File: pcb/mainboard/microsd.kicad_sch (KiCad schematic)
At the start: 11 parts, among them U700 W25Q128JVP

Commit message: Working on mainboard schematics
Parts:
- removed U?: NX3P1108UK, footprint:CSP-4_2x2_1.0x1.0mm, symbol symbols:NX3P1108UK
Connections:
- net +3V3 is gone; now on net +SD: C?.1
- net GND is gone; now on net +SD: C701.2, C703.1, C?.1, C?.2, CARD700.10, CARD700.11, CARD700.12, CARD700.13, CARD700.6 (VSS), U700.4 (GND), U700.9 (EP)
- net +SD: now reaches C701.1, CARD700.4 (VDD)
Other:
- moved on the sheet: C701, C?

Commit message: Mainboard schematics WIP
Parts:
- gave numbers to parts that had none: 3
- renumbered C703 to C702, C701 to C703, CARD700 to CARD701, R700 to R702, U700 to U702
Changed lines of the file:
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@@
   (symbol (lib_id "symbols:MICRO_SD(TFC-WPAPR-08)") (at 220.98 76.2 0) (unit 1)
     (in_bom yes) (on_board yes)
-    (property "Reference" "CARD700" (id 0) (at 229.311 73.584 0)
+    (property "Reference" "CARD701" (id 0) (at 229.311 73.584 0)
       (effects (font (size 1.524 1.524)) (justify left))
     )
@@
   (symbol (lib_id "power:GND") (at 210.82 88.9 0) (unit 1)
     (in_bom yes) (on_board yes)
-    (property "Reference" "#PWR0200" (id 0) (at 210.82 95.25 0)
+    (property "Reference" "#PWR0707" (id 0) (at 210.82 95.25 0)
       (effects (font (size 1.27 1.27)) hide)
     )
@@
   (symbol (lib_id "Device:R") (at 194.31 68.58 270) (unit 1)
     (in_bom yes) (on_board yes)
-    (property "Reference" "R700" (id 0) (at 189.23 67.31 90))
+    (property "Reference" "R702" (id 0) (at 189.23 67.31 90))
     (property "Value" "0" (id 1) (at 199.39 67.31 90))
     (property "Footprint" "Resistor_SMD:R_0402_1005Metric" (id 2) (at 194.31 66.802 90)
@@
   (symbol (lib_id "Device:C") (at 190.5 52.07 0) (unit 1)
     (in_bom yes) (on_board yes)
-    (property "Reference" "C701" (id 0) (at 193.421 50.902 0)
+    (property "Reference" "C703" (id 0) (at 193.421 50.902 0)
       (effects (font (size 1.27 1.27)) (justify left))
     )
@@
   (symbol (lib_id "power:GND") (at 190.5 55.88 0) (unit 1)
     (in_bom yes) (on_board yes)
-    (property "Reference" "#PWR0202" (id 0) (at 190.5 62.23 0)
+    (property "Reference" "#PWR0703" (id 0) (at 190.5 62.23 0)
       (effects (font (size 1.27 1.27)) hide)
     )
@@
   (symbol (lib_id "power:GND") (at 121.92 167.64 0) (unit 1)
     (in_bom yes) (on_board yes)
-    (property "Reference" "#PWR?" (id 0) (at 121.92 173.99 0)
+    (property "Reference" "#PWR0701" (id 0) (at 121.92 173.99 0)
       (effects (font (size 1.27 1.27)) hide)
     )
@@
   (symbol (lib_id "power:GND") (at 182.88 119.38 0) (unit 1)
     (in_bom yes) (on_board yes)
-    (property "Reference" "#PWR0245" (id 0) (at 182.88 125.73 0)
+    (property "Reference" "#PWR0702" (id 0) (at 182.88 125.73 0)
       (effects (font (size 1.27 1.27)) hide)
     )
@@
   (symbol (lib_id "Device:C") (at 115.57 165.1 270) (unit 1)
     (in_bom yes) (on_board yes)
-    (property "Reference" "C?" (id 0) (at 111.76 163.83 90))
+    (property "Reference" "C701" (id 0) (at 111.76 163.83 90))
     (property "Value" "18pF" (id 1) (at 120.65 163.83 90))
     (property "Footprint" "Capacitor_SMD:C_0402_1005Metric" (id 2) (at 111.76 166.0652 0)
@@
   (symbol (lib_id "symbols:MIMX8MN6DVTJZAA") (at 93.98 101.6 0) (unit 8)
     (in_bom yes) (on_board yes) (fields_autoplaced)
-    (property "Reference" "U?" (id 0) (at 93.98 101.6 0))
+    (property "Reference" "U201" (id 0) (at 93.98 101.6 0))
     (property "Value" "MIMX8MN6DVTJZAA" (id 1) (at 93.98 104.14 0))
     (property "Footprint" "footprint:BGA-486_27x27_14.0x14.0mm" (id 2) (at 93.98 101.6 0)
@@
   (symbol (lib_id "symbols:MIMX8MN6DVTJZAA") (at 96.52 48.26 0) (unit 9)
     (in_bom yes) (on_board yes) (fields_autoplaced)
-    (property "Reference" "U?" (id 0) (at 96.52 48.26 0))
+    (property "Reference" "U201" (id 0) (at 96.52 48.26 0))
     (property "Value" "MIMX8MN6DVTJZAA" (id 1) (at 96.52 50.8 0))
     (property "Footprint" "footprint:BGA-486_27x27_14.0x14.0mm" (id 2) (at 96.52 48.26 0)
@@
   (symbol (lib_id "Device:C") (at 182.88 115.57 180) (unit 1)
     (in_bom yes) (on_board yes)
-    (property "Reference" "C703" (id 0) (at 177.8 114.3 0))
+    (property "Reference" "C702" (id 0) (at 177.8 114.3 0))
     (property "Value" "470nF" (id 1) (at 177.8 116.84 0))
     (property "Footprint" "Capacitor_SMD:C_0402_1005Metric" (id 2) (at 181.9148 111.76 0)
@@
   (symbol (lib_id "Device:C") (at 199.39 52.07 0) (unit 1)
     (in_bom yes) (on_board yes)
-    (property "Reference" "C?" (id 0) (at 202.311 50.902 0)
+    (property "Reference" "C704" (id 0) (at 202.311 50.902 0)
       (effects (font (size 1.27 1.27)) (justify left))
     )
@@
   (symbol (lib_id "symbols:+SD") (at 208.28 48.26 0) (unit 1)
     (in_bom yes) (on_board yes)
-    (property "Reference" "#PWR?" (id 0) (at 208.28 52.07 0)
+    (property "Reference" "#PWR0704" (id 0) (at 208.28 52.07 0)
       (effects (font (size 1.27 1.27)) hide)
     )
@@
   (symbol (lib_id "power:+1V8") (at 208.28 111.76 0) (unit 1)
     (in_bom yes) (on_board yes) (fields_autoplaced)
-    (property "Reference" "#PWR?" (id 0) (at 208.28 115.57 0)
+    (property "Reference" "#PWR0705" (id 0) (at 208.28 115.57 0)
       (effects (font (size 1.27 1.27)) hide)
     )
@@
   (symbol (lib_id "Memory_Flash:W25Q32JVZP") (at 208.28 128.27 0) (unit 1)
     (in_bom yes) (on_board yes)
-    (property "Reference" "U700" (id 0) (at 215.9 116.053 0))
+    (property "Reference" "U702" (id 0) (at 215.9 116.053 0))
     (property "Value" "W25Q128JVP" (id 1) (at 215.9 118.364 0))
     (property "Footprint" "Package_SON:WSON-8-1EP_6x5mm_P1.27mm_EP3.4x4.3mm" (id 2) (at 208.28 128.27 0)
@@
   (symbol (lib_id "power:GND") (at 208.28 138.43 0) (unit 1)
     (in_bom yes) (on_board yes)
-    (property "Reference" "#PWR0247" (id 0) (at 208.28 144.78 0)
-      (effects (font (size 1.27 1.27)) hide)
-    )
+    (property "Reference" "#PWR0706" (id 0) (at 208.28 144.78 0)
+      (effects (font (size 1.27 1.27)) hide)
+    )

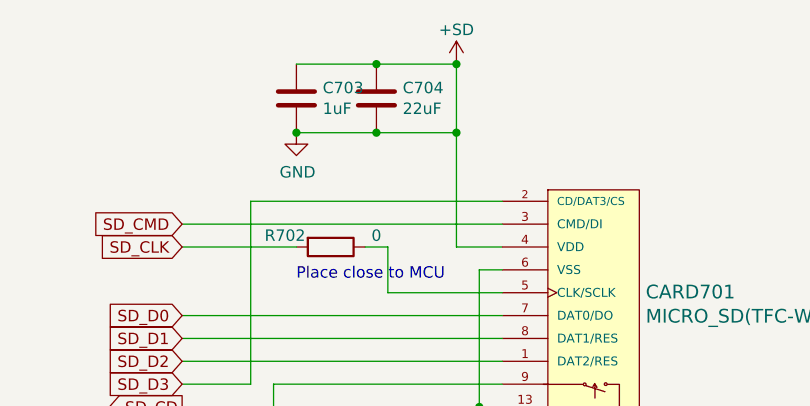
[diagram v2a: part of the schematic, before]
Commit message: Draft motherboard schematics for r0.0 layout
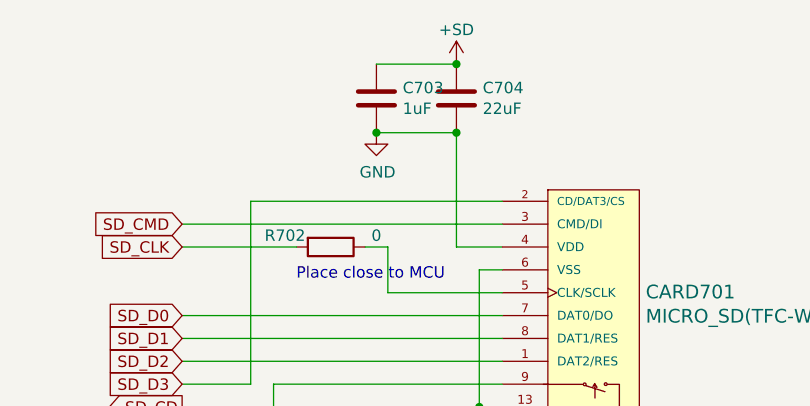
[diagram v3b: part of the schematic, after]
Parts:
- R701: footprint Capacitor_SMD:C_0402_1005Metric -> Resistor_SMD:R_0402_1005Metric
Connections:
- net +SD: no longer C701.1, C702.1, C703.2, C704.2, CARD701.10, CARD701.11, CARD701.12, CARD701.13, CARD701.4 (VDD), CARD701.6 (VSS), U702.4 (GND), U702.9 (EP)
- new net GND: C701.1, C702.1, C703.2, C704.2, CARD701.10, CARD701.11, CARD701.12, CARD701.13, CARD701.4 (VDD), CARD701.6 (VSS), U702.4 (GND), U702.9 (EP)
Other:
- moved on the sheet: C703, C704
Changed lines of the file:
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@@
   (junction (at 208.28 138.43) (diameter 0.9144) (color 0 0 0 0)
   )
-  (junction (at 199.39 48.26) (diameter 0) (color 0 0 0 0)
-  )
   (junction (at 208.28 48.26) (diameter 0) (color 0 0 0 0)
-  )
-  (junction (at 190.5 55.88) (diameter 0) (color 0 0 0 0)
   )
   (junction (at 210.82 86.36) (diameter 0.9144) (color 0 0 0 0)
@@
     (stroke (width 0) (type default) (color 0 0 0 0))
   )
-  (wire (pts (xy 208.28 55.88) (xy 208.28 48.26))
-    (stroke (width 0) (type solid) (color 0 0 0 0))
-  )
   (wire (pts (xy 121.92 165.1) (xy 121.92 167.64))
     (stroke (width 0) (type default) (color 0 0 0 0))
@@
     (stroke (width 0) (type solid) (color 0 0 0 0))
   )
-  (wire (pts (xy 190.5 48.26) (xy 199.39 48.26))
-    (stroke (width 0) (type default) (color 0 0 0 0))
-  )
   (wire (pts (xy 200.66 68.58) (xy 200.66 73.66))
     (stroke (width 0) (type solid) (color 0 0 0 0))
@@
   (wire (pts (xy 220.98 133.35) (xy 226.06 133.35))
     (stroke (width 0) (type solid) (color 0 0 0 0))
-  )
-  (wire (pts (xy 190.5 55.88) (xy 199.39 55.88))
-    (stroke (width 0) (type default) (color 0 0 0 0))
   )
   (wire (pts (xy 116.84 83.82) (xy 119.38 83.82))
@@
     (pin "2")
   )
-  (symbol (lib_id "Device:C") (at 190.5 52.07 0) (unit 1)
+  (symbol (lib_id "Device:C") (at 199.39 52.07 0) (unit 1)
     (in_bom yes) (on_board yes)
-    (property "Reference" "C703" (id 0) (at 193.421 50.902 0)
+    (property "Reference" "C703" (id 0) (at 202.311 50.902 0)
       (effects (font (size 1.27 1.27)) (justify left))
     )
-    (property "Value" "1uF" (id 1) (at 193.421 53.213 0)
+    (property "Value" "1uF" (id 1) (at 202.311 53.213 0)
       (effects (font (size 1.27 1.27)) (justify left))
     )
-    (property "Footprint" "Capacitor_SMD:C_0402_1005Metric" (id 2) (at 191.4652 55.88 0)
-      (effects (font (size 1.27 1.27)) hide)
-    )
-    (property "Datasheet" "~" (id 3) (at 190.5 52.07 0)
+    (property "Footprint" "Capacitor_SMD:C_0402_1005Metric" (id 2) (at 200.3552 55.88 0)
+      (effects (font (size 1.27 1.27)) hide)
+    )
+    (property "Datasheet" "~" (id 3) (at 199.39 52.07 0)
       (effects (font (size 1.27 1.27)) hide)
     )
@@
     (pin "2")
   )
-  (symbol (lib_id "power:GND") (at 190.5 55.88 0) (unit 1)
+  (symbol (lib_id "power:GND") (at 199.39 55.88 0) (unit 1)
     (in_bom yes) (on_board yes)
-    (property "Reference" "#PWR0703" (id 0) (at 190.5 62.23 0)
-      (effects (font (size 1.27 1.27)) hide)
-    )
-    (property "Value" "GND" (id 1) (at 190.627 60.2742 0))
-    (property "Footprint" "" (id 2) (at 190.5 55.88 0)
-      (effects (font (size 1.27 1.27)) hide)
-    )
-    (property "Datasheet" "" (id 3) (at 190.5 55.88 0)
+    (property "Reference" "#PWR0703" (id 0) (at 199.39 62.23 0)
+      (effects (font (size 1.27 1.27)) hide)
+    )
+    (property "Value" "GND" (id 1) (at 199.517 60.2742 0))
+    (property "Footprint" "" (id 2) (at 199.39 55.88 0)
+      (effects (font (size 1.27 1.27)) hide)
+    )
+    (property "Datasheet" "" (id 3) (at 199.39 55.88 0)
       (effects (font (size 1.27 1.27)) hide)
     )
@@
     (property "Reference" "R701" (id 0) (at 189.23 114.3 0))
     (property "Value" "100K" (id 1) (at 189.23 116.84 0))
-    (property "Footprint" "Capacitor_SMD:C_0402_1005Metric" (id 2) (at 191.262 115.57 90)
+    (property "Footprint" "Resistor_SMD:R_0402_1005Metric" (id 2) (at 191.262 115.57 90)
       (effects (font (size 1.27 1.27)) hide)
     )
@@
     (pin "2")
   )
-  (symbol (lib_id "Device:C") (at 199.39 52.07 0) (unit 1)
+  (symbol (lib_id "Device:C") (at 208.28 52.07 0) (unit 1)
     (in_bom yes) (on_board yes)
-    (property "Reference" "C704" (id 0) (at 202.311 50.902 0)
+    (property "Reference" "C704" (id 0) (at 211.201 50.902 0)
       (effects (font (size 1.27 1.27)) (justify left))
     )
-    (property "Value" "22uF" (id 1) (at 202.311 53.213 0)
+    (property "Value" "22uF" (id 1) (at 211.201 53.213 0)
       (effects (font (size 1.27 1.27)) (justify left))
     )
-    (property "Footprint" "Capacitor_SMD:C_0603_1608Metric" (id 2) (at 200.3552 55.88 0)
-      (effects (font (size 1.27 1.27)) hide)
-    )
-    (property "Datasheet" "~" (id 3) (at 199.39 52.07 0)
-      (effects (font (size 1.27 1.27)) hide)
-    )
+    (property "Footprint" "Capacitor_SMD:C_0603_1608Metric" (id 2) (at 209.2452 55.88 0)
+      (effects (font (size 1.27 1.27)) hide)
+    )
+    (property "Datasheet" "~" (id 3) (at 208.28 52.07 0)
+      (effects (font (size 1.27 1.27)) hide)
+    )

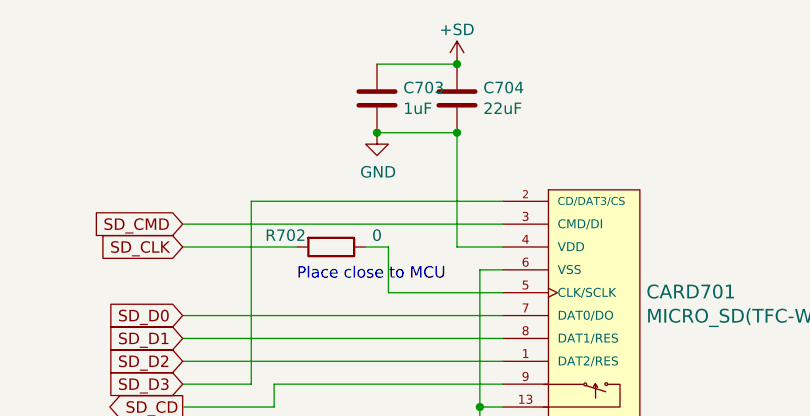
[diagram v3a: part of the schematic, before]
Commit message: Motherboard PCB component initial placement, schematics fixes
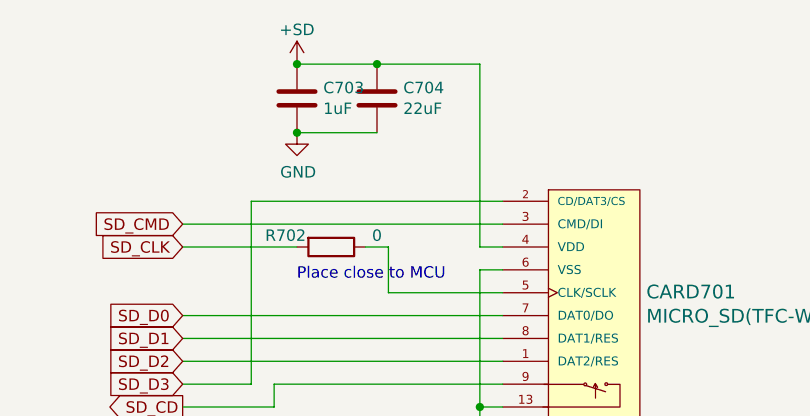
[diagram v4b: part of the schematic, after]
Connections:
- net +SD: now also CARD701.4 (VDD)
- net GND: no longer CARD701.4 (VDD)
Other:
- moved on the sheet: C703, C704
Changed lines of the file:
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@@
   (junction (at 208.28 111.76) (diameter 0) (color 0 0 0 0)
   )
-  (junction (at 199.39 55.88) (diameter 0) (color 0 0 0 0)
+  (junction (at 190.5 55.88) (diameter 0) (color 0 0 0 0)
   )
   (junction (at 208.28 138.43) (diameter 0.9144) (color 0 0 0 0)
   )
-  (junction (at 208.28 48.26) (diameter 0) (color 0 0 0 0)
+  (junction (at 190.5 48.26) (diameter 0) (color 0 0 0 0)
+  )
+  (junction (at 199.39 48.26) (diameter 0) (color 0 0 0 0)
   )
   (junction (at 210.82 86.36) (diameter 0.9144) (color 0 0 0 0)
   )
   (junction (at 193.04 111.76) (diameter 0.9144) (color 0 0 0 0)
-  )
-  (junction (at 208.28 55.88) (diameter 0) (color 0 0 0 0)
   )
   (no_connect (at 109.22 137.16))
@@
     (stroke (width 0) (type solid) (color 0 0 0 0))
   )
-  (wire (pts (xy 199.39 48.26) (xy 208.28 48.26))
+  (wire (pts (xy 199.39 48.26) (xy 210.82 48.26))
     (stroke (width 0) (type default) (color 0 0 0 0))
   )
@@
     (stroke (width 0) (type default) (color 0 0 0 0))
   )
-  (wire (pts (xy 199.39 55.88) (xy 208.28 55.88))
-    (stroke (width 0) (type default) (color 0 0 0 0))
-  )
-  (wire (pts (xy 208.28 68.58) (xy 213.36 68.58))
-    (stroke (width 0) (type solid) (color 0 0 0 0))
+  (wire (pts (xy 190.5 55.88) (xy 199.39 55.88))
+    (stroke (width 0) (type default) (color 0 0 0 0))
   )
   (wire (pts (xy 200.66 68.58) (xy 200.66 73.66))
     (stroke (width 0) (type solid) (color 0 0 0 0))
   )
+  (wire (pts (xy 213.36 68.58) (xy 210.82 68.58))
+    (stroke (width 0) (type default) (color 0 0 0 0))
+  )
   (wire (pts (xy 109.22 142.24) (xy 111.76 142.24))
     (stroke (width 0) (type solid) (color 0 0 0 0))
@@
     (stroke (width 0) (type solid) (color 0 0 0 0))
   )
+  (wire (pts (xy 190.5 48.26) (xy 199.39 48.26))
+    (stroke (width 0) (type default) (color 0 0 0 0))
+  )
   (wire (pts (xy 116.84 83.82) (xy 119.38 83.82))
     (stroke (width 0) (type default) (color 0 0 0 0))
@@
     (stroke (width 0) (type default) (color 0 0 0 0))
   )
-  (wire (pts (xy 208.28 68.58) (xy 208.28 55.88))
-    (stroke (width 0) (type solid) (color 0 0 0 0))
+  (wire (pts (xy 210.82 68.58) (xy 210.82 48.26))
+    (stroke (width 0) (type default) (color 0 0 0 0))
   )
   (wire (pts (xy 177.8 81.28) (xy 213.36 81.28))
@@
     (pin "2")
   )
-  (symbol (lib_id "Device:C") (at 199.39 52.07 0) (unit 1)
+  (symbol (lib_id "Device:C") (at 190.5 52.07 0) (unit 1)
     (in_bom yes) (on_board yes)
-    (property "Reference" "C703" (id 0) (at 202.311 50.902 0)
+    (property "Reference" "C703" (id 0) (at 193.421 50.902 0)
       (effects (font (size 1.27 1.27)) (justify left))
     )
-    (property "Value" "1uF" (id 1) (at 202.311 53.213 0)
+    (property "Value" "1uF" (id 1) (at 193.421 53.213 0)
       (effects (font (size 1.27 1.27)) (justify left))
     )
-    (property "Footprint" "Capacitor_SMD:C_0402_1005Metric" (id 2) (at 200.3552 55.88 0)
-      (effects (font (size 1.27 1.27)) hide)
-    )
-    (property "Datasheet" "~" (id 3) (at 199.39 52.07 0)
+    (property "Footprint" "Capacitor_SMD:C_0402_1005Metric" (id 2) (at 191.4652 55.88 0)
+      (effects (font (size 1.27 1.27)) hide)
+    )
+    (property "Datasheet" "~" (id 3) (at 190.5 52.07 0)
       (effects (font (size 1.27 1.27)) hide)
     )
@@
     (pin "2")
   )
-  (symbol (lib_id "power:GND") (at 199.39 55.88 0) (unit 1)
+  (symbol (lib_id "power:GND") (at 190.5 55.88 0) (unit 1)
     (in_bom yes) (on_board yes)
-    (property "Reference" "#PWR0703" (id 0) (at 199.39 62.23 0)
-      (effects (font (size 1.27 1.27)) hide)
-    )
-    (property "Value" "GND" (id 1) (at 199.517 60.2742 0))
-    (property "Footprint" "" (id 2) (at 199.39 55.88 0)
-      (effects (font (size 1.27 1.27)) hide)
-    )
-    (property "Datasheet" "" (id 3) (at 199.39 55.88 0)
+    (property "Reference" "#PWR0703" (id 0) (at 190.5 62.23 0)
+      (effects (font (size 1.27 1.27)) hide)
+    )
+    (property "Value" "GND" (id 1) (at 190.627 60.2742 0))
+    (property "Footprint" "" (id 2) (at 190.5 55.88 0)
+      (effects (font (size 1.27 1.27)) hide)
+    )
+    (property "Datasheet" "" (id 3) (at 190.5 55.88 0)
       (effects (font (size 1.27 1.27)) hide)
     )
@@
     (pin "2")
   )
-  (symbol (lib_id "Device:C") (at 208.28 52.07 0) (unit 1)
+  (symbol (lib_id "Device:C") (at 199.39 52.07 0) (unit 1)
     (in_bom yes) (on_board yes)
-    (property "Reference" "C704" (id 0) (at 211.201 50.902 0)
+    (property "Reference" "C704" (id 0) (at 202.311 50.902 0)
       (effects (font (size 1.27 1.27)) (justify left))
     )
-    (property "Value" "22uF" (id 1) (at 211.201 53.213 0)
+    (property "Value" "22uF" (id 1) (at 202.311 53.213 0)
       (effects (font (size 1.27 1.27)) (justify left))
     )
-    (property "Footprint" "Capacitor_SMD:C_0603_1608Metric" (id 2) (at 209.2452 55.88 0)
-      (effects (font (size 1.27 1.27)) hide)
-    )
-    (property "Datasheet" "~" (id 3) (at 208.28 52.07 0)
+    (property "Footprint" "Capacitor_SMD:C_0603_1608Metric" (id 2) (at 200.3552 55.88 0)
+      (effects (font (size 1.27 1.27)) hide)
+    )
+    (property "Datasheet" "~" (id 3) (at 199.39 52.07 0)
       (effects (font (size 1.27 1.27)) hide)
     )
@@
     (pin "2")
   )
-  (symbol (lib_id "symbols:+SD") (at 208.28 48.26 0) (unit 1)
+  (symbol (lib_id "symbols:+SD") (at 190.5 48.26 0) (unit 1)
     (in_bom yes) (on_board yes)
-    (property "Reference" "#PWR0704" (id 0) (at 208.28 52.07 0)
-      (effects (font (size 1.27 1.27)) hide)
-    )
-    (property "Value" "+SD" (id 1) (at 208.28 44.45 0))
-    (property "Footprint" "" (id 2) (at 208.28 48.26 0)
-      (effects (font (size 1.27 1.27)) hide)
-    )
-    (property "Datasheet" "" (id 3) (at 208.28 48.26 0)
-      (effects (font (size 1.27 1.27)) hide)
-    )
+    (property "Reference" "#PWR0704" (id 0) (at 190.5 52.07 0)
+      (effects (font (size 1.27 1.27)) hide)
+    )
+    (property "Value" "+SD" (id 1) (at 190.5 44.45 0))
+    (property "Footprint" "" (id 2) (at 190.5 48.26 0)
+      (effects (font (size 1.27 1.27)) hide)
+    )
+    (property "Datasheet" "" (id 3) (at 190.5 48.26 0)
+      (effects (font (size 1.27 1.27)) hide)
+    )
